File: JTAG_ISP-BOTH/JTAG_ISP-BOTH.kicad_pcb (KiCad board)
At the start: 2 copper layers, 48.8 x 46.1 mm, 19 parts, among them J1 Conn_01x08, J1 Conn_02x03_Counter_Clockwise, J2 Conn_01x08, J3 Conn_01x08

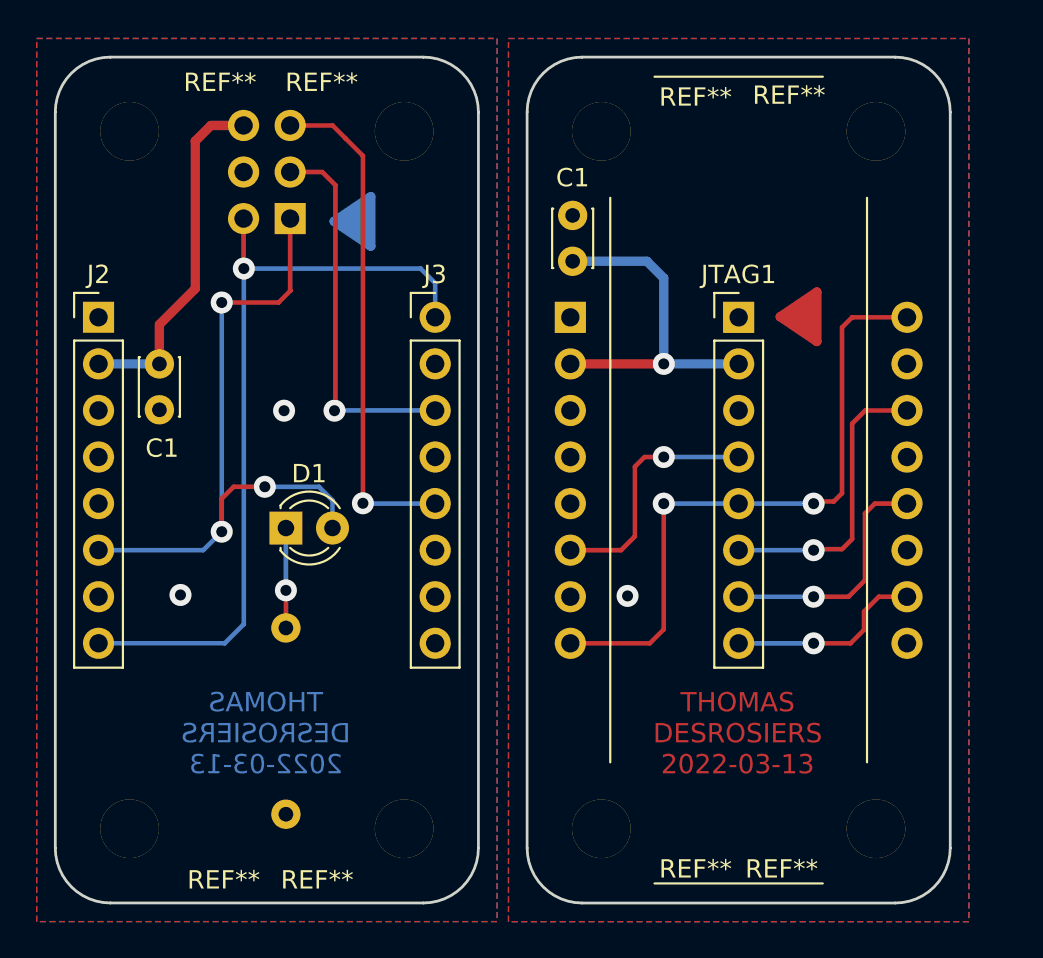
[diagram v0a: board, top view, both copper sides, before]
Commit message: ~ Mise à jour des 2 PCB dans le projet BOTH qui est utilisé pour combiner les projets ISP et HDR pour la fabrication.
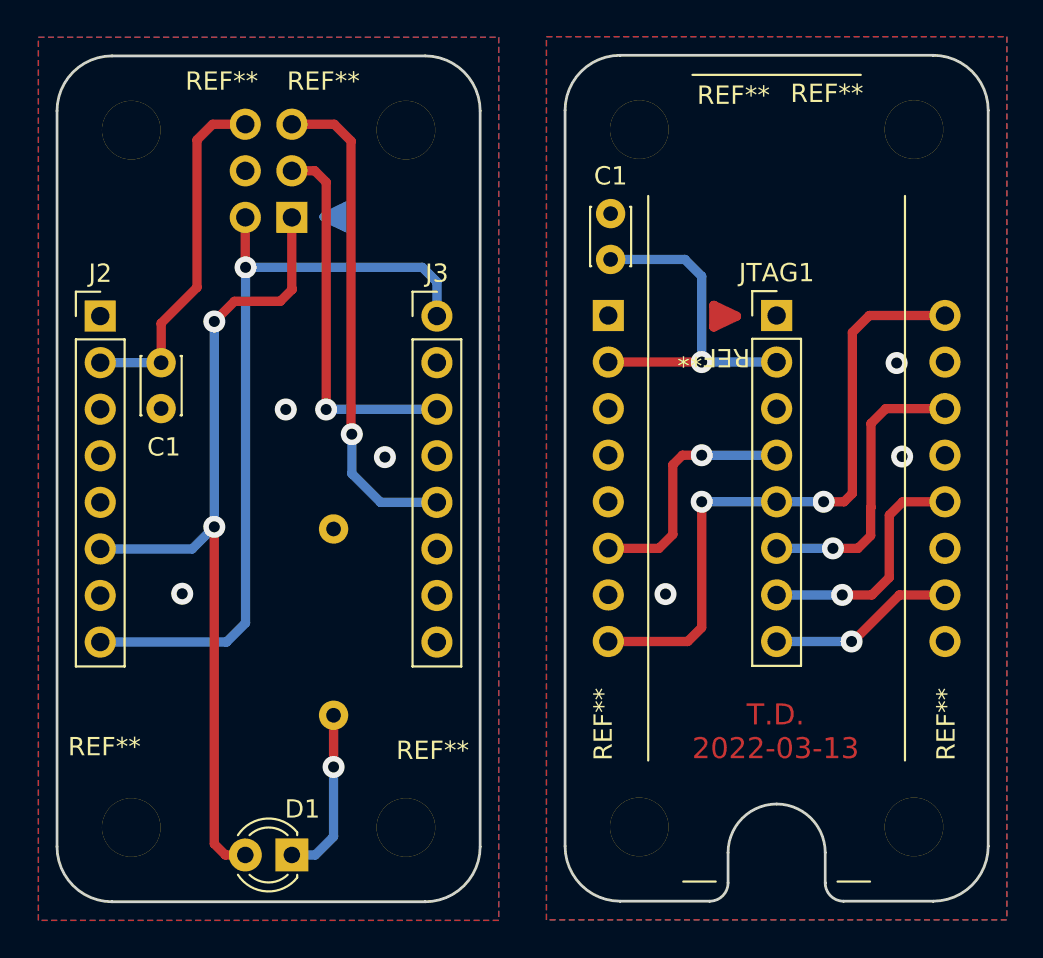
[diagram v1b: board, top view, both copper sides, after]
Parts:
- removed the C1 at (150.5, 78.0)
- removed the C1 at (173.0, 72.5)
- removed the J1 at (172.9, 75.5)
- removed the J1 at (157.6, 70.1)
- removed the J2 at (147.2, 75.5)
- removed the J2 at (191.3, 75.5)
- removed the REF** at (163.8, 103.4)
- removed the REF** at (174.6, 103.4)
- removed the REF** at (163.8, 65.4)
- removed the REF** at (148.9, 103.4)
- removed the REF** at (189.6, 103.4)
- removed the REF** at (174.6, 65.4)
- removed the REF** at (189.6, 65.4)
- removed the REF** at (148.9, 65.4)
- removed the REF** at (161.3, 70.6)
- added C1: 100nF, Capacitor_THT:C_Disc_D3.0mm_W2.0mm_P2.50mm, F.Cu at (175.1, 72.3)
- added C1: 100nF, Capacitor_THT:C_Disc_D3.0mm_W2.0mm_P2.50mm, F.Cu at (150.6, 78.0)
- added J1: Conn_01x08, Connector_PinHeader_2.54mm:PinHeader_1x08_P2.54mm_Vertical, B.Cu at (175.0, 75.4)
- added J1: Conn_02x03_Counter_Clockwise, Connector_PinSocket_2.54mm:PinSocket_2x03_P2.54mm_Vertical, B.Cu at (157.7, 70.1)
- added J2: Conn_01x08, Connector_PinHeader_2.54mm:PinHeader_1x08_P2.54mm_Vertical, F.Cu at (147.3, 75.4)
- added J2: Conn_01x08, Connector_PinHeader_2.54mm:PinHeader_1x08_P2.54mm_Vertical, B.Cu at (193.3, 75.4)
- added REF**: MountingHole_3.2mm_M3, MountingHole:MountingHole_3.2mm_M3, F.Cu at (163.9, 65.3)
- added REF**: Fleche_small, THOMAS_library:Fleche_small, B.Cu at (160.7, 70.4)
- added REF**: MountingHole_3.2mm_M3, MountingHole:MountingHole_3.2mm_M3, F.Cu at (176.7, 103.3)
- added REF**: MountingHole_3.2mm_M3, MountingHole:MountingHole_3.2mm_M3, F.Cu at (191.7, 103.3)
- added REF**: MountingHole_3.2mm_M3, MountingHole:MountingHole_3.2mm_M3, F.Cu at (163.9, 103.3)
- added REF**: MountingHole_3.2mm_M3, MountingHole:MountingHole_3.2mm_M3, F.Cu at (176.7, 65.3)
- added REF**: Fleche_small, THOMAS_library:Fleche_small, F.Cu at (180.7, 75.8)
- added REF**: MountingHole_3.2mm_M3, MountingHole:MountingHole_3.2mm_M3, F.Cu at (149.0, 103.3)
- added REF**: MountingHole_3.2mm_M3, MountingHole:MountingHole_3.2mm_M3, F.Cu at (149.0, 65.3)
- added REF**: MountingHole_3.2mm_M3, MountingHole:MountingHole_3.2mm_M3, F.Cu at (191.7, 65.3)
- moved D1 17.8 mm to (157.7, 104.8), turned to 180 degrees
- moved R1 5.43 mm to (160.0, 97.2), turned to 90 degrees
- moved JTAG1 2.07 mm to (184.2, 75.4)
- moved J3 0.11 mm to (165.6, 75.4)
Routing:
- net MISO: track 37.7 -> 46.1 mm, vias 3 -> 2
- net Net-(D1-Pad1): track 5.25 -> 9.31 mm
- net (no net): track 88.8 -> 87.3 mm
- net GND: vias 3 -> 6
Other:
- board size 48.8 x 46.1 mm -> 50.8 x 46.2 mm
- board text added: "T.D. 2022-03-13"
- board text removed: "THOMAS DESROSIERS 2022-03-13"

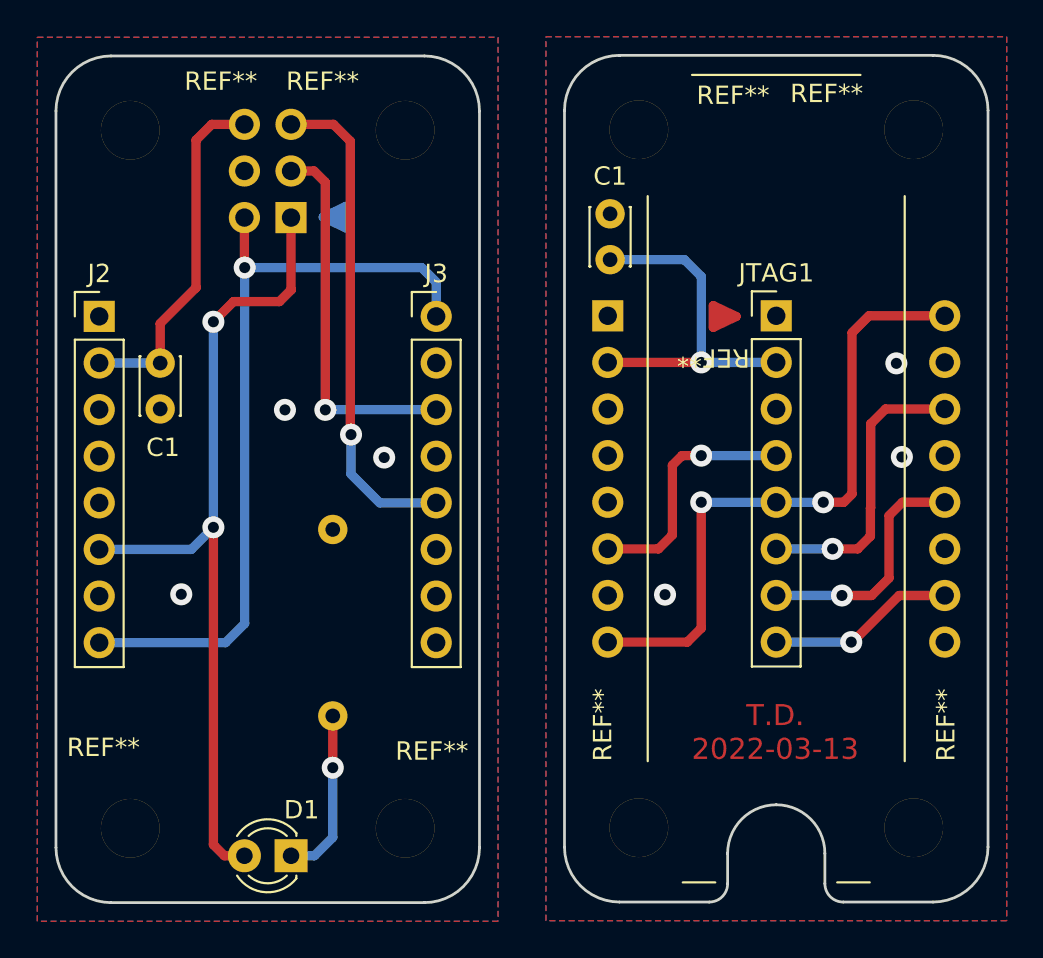
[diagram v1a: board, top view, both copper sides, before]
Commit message: # [PCB] * Mise à jour des fichiers gerbers du projet BOTH. + Création d'une archive PROD_LPKF.zip qui contient les fichiers envoyés pour fabrication. - Suppression du fichier .round-tracks-config qui est inutile. * Mise à jours de la cartouche pour les 2 projets.     * Date actuelle.     * Version actuelle.     * Titre du projet.
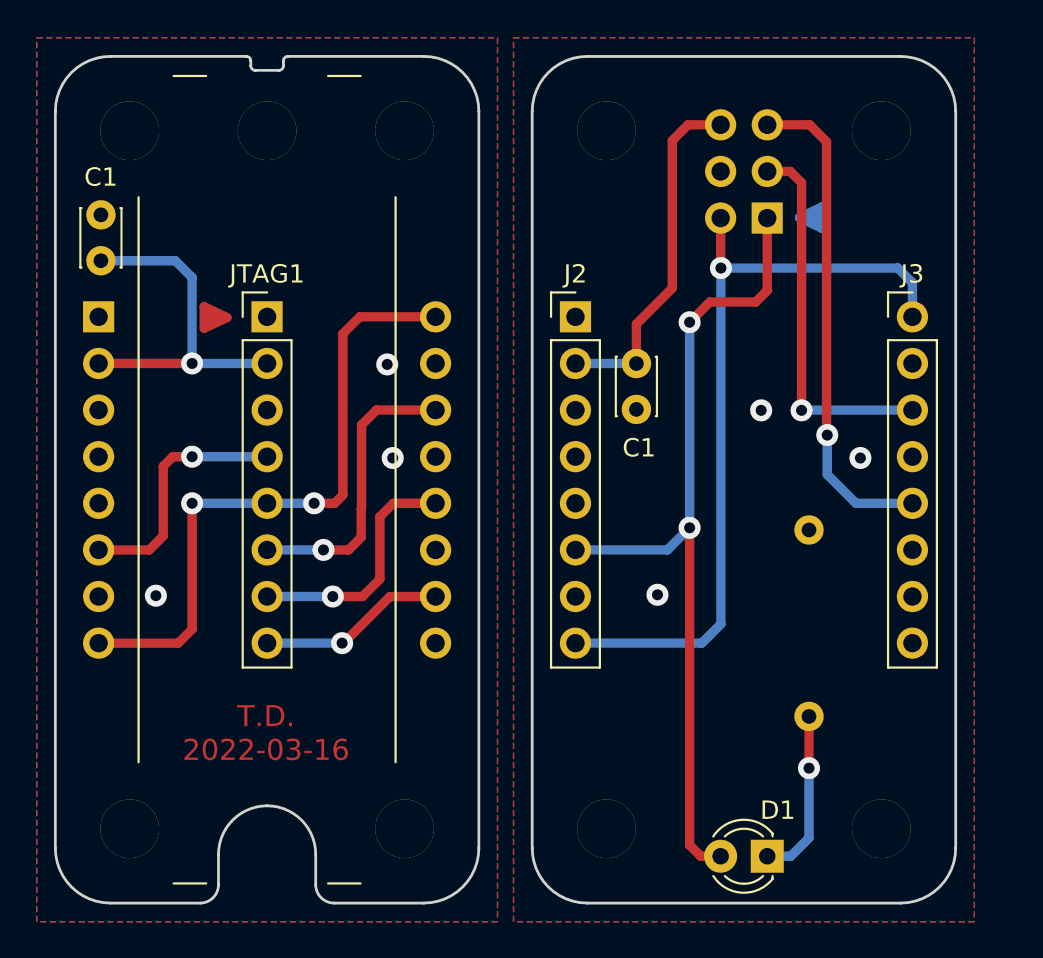
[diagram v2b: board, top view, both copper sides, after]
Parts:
- removed the C1 at (175.1, 72.3)
- removed the C1 at (150.6, 78.0)
- removed the J1 at (175.0, 75.4)
- removed the J1 at (157.7, 70.1)
- removed the J2 at (147.3, 75.4)
- removed the J2 at (193.3, 75.4)
- removed the REF** at (163.9, 65.3)
- removed the REF** at (160.7, 70.4)
- removed the REF** at (176.7, 103.3)
- removed the REF** at (191.7, 103.3)
- removed the REF** at (163.9, 103.3)
- removed the REF** at (176.7, 65.3)
- removed the REF** at (180.7, 75.8)
- removed the REF** at (149.0, 103.3)
- removed the REF** at (149.0, 65.3)
- removed the REF** at (191.7, 65.3)
- added C1: 100nF, Capacitor_THT:C_Disc_D3.0mm_W2.0mm_P2.50mm, F.Cu at (147.4, 72.4)
- added C1: 100nF, Capacitor_THT:C_Disc_D3.0mm_W2.0mm_P2.50mm, F.Cu at (176.5, 78.0)
- added J1: Conn_02x03_Counter_Clockwise, Connector_PinSocket_2.54mm:PinSocket_2x03_P2.54mm_Vertical, B.Cu at (183.7, 70.1)
- added J1: Conn_01x08, Connector_PinHeader_2.54mm:PinHeader_1x08_P2.54mm_Vertical, B.Cu at (147.2, 75.5)
- added J2: Conn_01x08, Connector_PinHeader_2.54mm:PinHeader_1x08_P2.54mm_Vertical, F.Cu at (173.2, 75.5)
- added J2: Conn_01x08, Connector_PinHeader_2.54mm:PinHeader_1x08_P2.54mm_Vertical, B.Cu at (165.6, 75.5)
- added REF**: MountingHole_3.2mm_M3, MountingHole:MountingHole_3.2mm_M3, F.Cu at (156.4, 65.3)
- added REF**: Fleche_small, THOMAS_library:Fleche_small, F.Cu at (153.0, 75.9)
- added REF**: Fleche_small, THOMAS_library:Fleche_small, B.Cu at (186.7, 70.4)
- added REF**: MountingHole_3.2mm_M3, MountingHole:MountingHole_3.2mm_M3, F.Cu at (174.9, 65.3)
- added REF**: MountingHole_3.2mm_M3, MountingHole:MountingHole_3.2mm_M3, F.Cu at (163.9, 65.3)
- added REF**: MountingHole_3.2mm_M3, MountingHole:MountingHole_3.2mm_M3, F.Cu at (148.9, 65.3)
- added REF**: MountingHole_3.2mm_M3, MountingHole:MountingHole_3.2mm_M3, F.Cu at (189.9, 103.4)
- added REF**: MountingHole_3.2mm_M3, MountingHole:MountingHole_3.2mm_M3, F.Cu at (148.9, 103.4)
- added REF**: MountingHole_3.2mm_M3, MountingHole:MountingHole_3.2mm_M3, F.Cu at (174.9, 103.4)
- added REF**: MountingHole_3.2mm_M3, MountingHole:MountingHole_3.2mm_M3, F.Cu at (189.9, 65.3)
- added REF**: MountingHole_3.2mm_M3, MountingHole:MountingHole_3.2mm_M3, F.Cu at (163.9, 103.4)
- moved JTAG1 27.7 mm to (156.4, 75.5)
- moved D1 26.0 mm to (183.7, 104.9)
- moved J3 26.0 mm to (191.6, 75.5)
- moved R1 26.0 mm to (185.9, 97.2)
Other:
- board size 50.8 x 46.2 mm -> 49.1 x 46.1 mm
- board text added: "T.D. 2022-03-16"
- board text removed: "T.D. 2022-03-13"

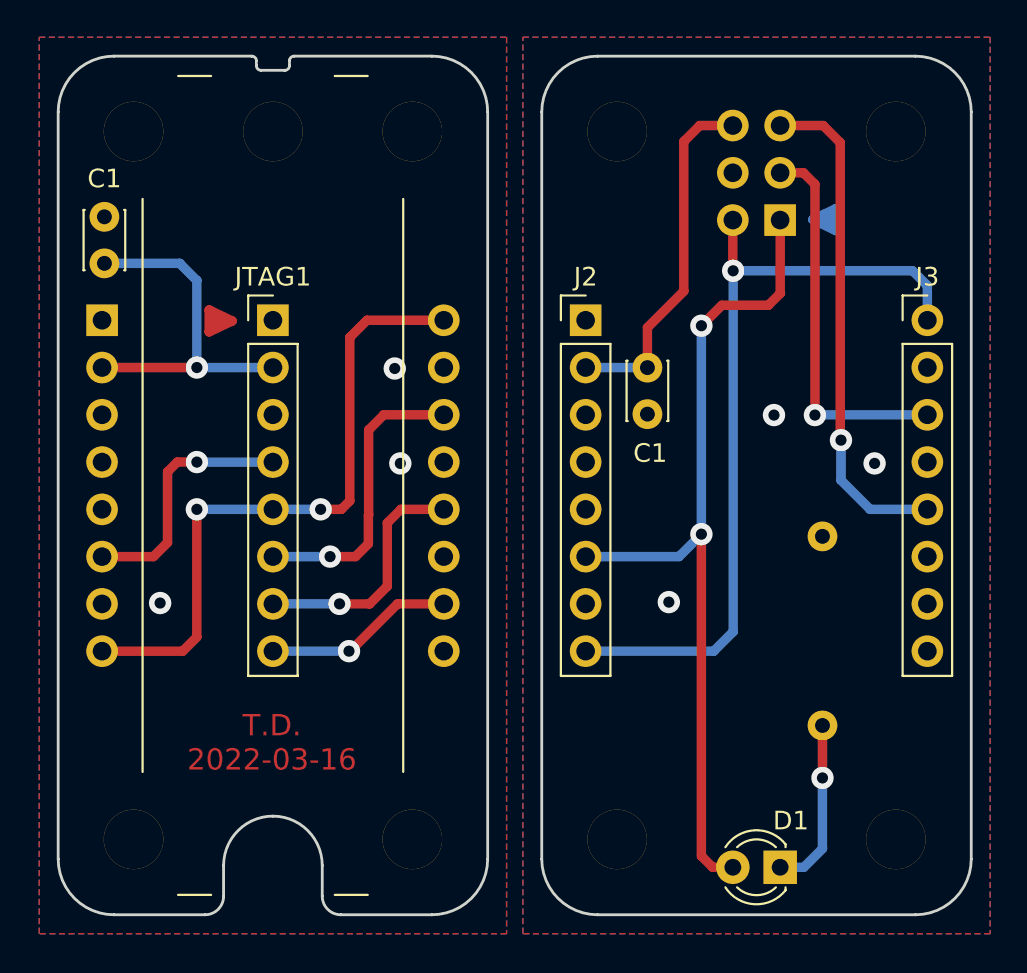
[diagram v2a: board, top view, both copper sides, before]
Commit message: # [PCB] + Création d'une archive PROD_LPKF.zip qui contient les fichiers envoyés pour fabrication. * Mise à jour des fichiers gerbers du projet BOTH. * Mise à jour de la cartouche pour le projet BOTH.     * Date actuelle.     * Version actuelle.
# [SCHÉMA]
- Suppression du fichier de schéma puisque ce projet est utilisé seulement pour combiner les 2 PCB.
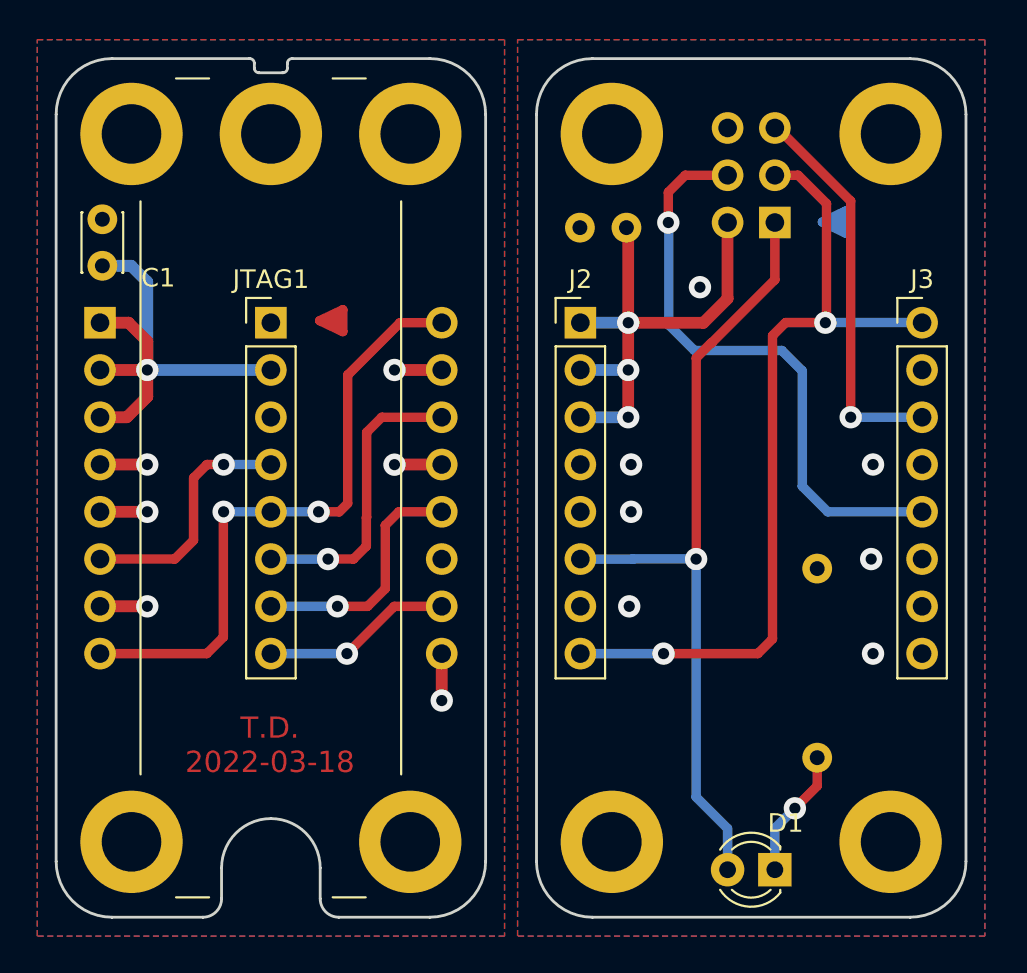
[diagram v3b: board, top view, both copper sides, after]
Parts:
- removed the C1 at (147.4, 72.4)
- removed the C1 at (176.5, 78.0)
- removed the J1 at (183.7, 70.1)
- removed the J1 at (147.2, 75.5)
- removed the J2 at (173.2, 75.5)
- removed the J2 at (165.6, 75.5)
- removed the REF** at (156.4, 65.3)
- removed the REF** at (153.0, 75.9)
- removed the REF** at (186.7, 70.4)
- removed the REF** at (174.9, 65.3)
- removed the REF** at (163.9, 65.3)
- removed the REF** at (148.9, 65.3)
- removed the REF** at (189.9, 103.4)
- removed the REF** at (148.9, 103.4)
- removed the REF** at (174.9, 103.4)
- removed the REF** at (189.9, 65.3)
- removed the REF** at (163.9, 103.4)
- added C1: 100nF, Capacitor_THT:C_Disc_D3.0mm_W2.0mm_P2.50mm, F.Cu at (147.3, 72.5)
- added C1: 100nF, Capacitor_THT:C_Disc_D3.0mm_W2.0mm_P2.50mm, B.Cu at (175.4, 70.5)
- added J1: Conn_02x03_Odd_Even, Connector_PinSocket_2.54mm:PinSocket_2x03_P2.54mm_Vertical, B.Cu at (183.4, 70.2)
- added J1: Conn_01x08, Connector_PinHeader_2.54mm:PinHeader_1x08_P2.54mm_Vertical, B.Cu at (147.1, 75.6)
- added J2: Conn_01x08, Connector_PinHeader_2.54mm:PinHeader_1x08_P2.54mm_Vertical, F.Cu at (172.9, 75.6)
- added J2: Conn_01x08, Connector_PinHeader_2.54mm:PinHeader_1x08_P2.54mm_Vertical, B.Cu at (165.5, 75.6)
- added REF**: MountingHole_3.2mm_M3_ISO14580_Pad, MountingHole:MountingHole_3.2mm_M3_ISO14580_Pad, F.Cu at (189.6, 65.5)
- added REF**: MountingHole_3.2mm_M3_ISO14580_Pad, MountingHole:MountingHole_3.2mm_M3_ISO14580_Pad, F.Cu at (163.8, 103.5)
- added REF**: Fleche_small, THOMAS_library:Fleche_small, B.Cu at (187.2, 70.5)
- added REF**: MountingHole_3.2mm_M3_ISO14580_Pad, MountingHole:MountingHole_3.2mm_M3_ISO14580_Pad, F.Cu at (148.8, 65.5)
- added REF**: MountingHole_3.2mm_M3_ISO14580_Pad, MountingHole:MountingHole_3.2mm_M3_ISO14580_Pad, F.Cu at (148.8, 103.5)
- added REF**: MountingHole_3.2mm_M3_ISO14580_Pad, MountingHole:MountingHole_3.2mm_M3_ISO14580_Pad, F.Cu at (189.6, 103.5)
- added REF**: MountingHole_3.2mm_M3_ISO14580_Pad, MountingHole:MountingHole_3.2mm_M3_ISO14580_Pad, F.Cu at (156.3, 65.5)
- added REF**: MountingHole_3.2mm_M3_ISO14580_Pad, MountingHole:MountingHole_3.2mm_M3_ISO14580_Pad, F.Cu at (174.6, 103.5)
- added REF**: Fleche_small, THOMAS_library:Fleche_small, F.Cu at (160.2, 75.1)
- added REF**: MountingHole_3.2mm_M3_ISO14580_Pad, MountingHole:MountingHole_3.2mm_M3_ISO14580_Pad, F.Cu at (174.6, 65.5)
- added REF**: MountingHole_3.2mm_M3_ISO14580_Pad, MountingHole:MountingHole_3.2mm_M3_ISO14580_Pad, F.Cu at (163.8, 65.5)
- moved R1 1.75 mm to (185.7, 99.0)
- moved D1 0.31 mm to (183.4, 105.0)
- moved J3 0.31 mm to (191.3, 75.6)
- moved JTAG1 0.17 mm to (156.3, 75.6)
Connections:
- J3 pad 2: unconnected-(J3-Pad2) -> GND
- J3 pad 4: unconnected-(J3-Pad4) -> GND
- J3 pad 6: unconnected-(J3-Pad6) -> GND
- J3 pad 8: unconnected-(J3-Pad8) -> GND
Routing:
- net GND: track 0.00 -> 15.2 mm, vias 6 -> 13
- net +5V: track 38.5 -> 53.7 mm, vias 1 -> 4
- net MOSI: track 27.1 -> 32.1 mm
- net MISO: track 46.1 -> 43.5 mm, vias 2 -> 1
- net Net-(D1-Pad1): track 9.31 -> 6.96 mm
- net SCLK: track 43.1 -> 45.1 mm, vias 1 -> 2
- net (no net): track 87.3 -> 85.9 mm
- net RESET: track 20.6 -> 21.1 mm
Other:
- board size 49.1 x 46.1 mm -> 48.9 x 46.1 mm
- board text added: "T.D. 2022-03-18"
- board text removed: "T.D. 2022-03-16"
